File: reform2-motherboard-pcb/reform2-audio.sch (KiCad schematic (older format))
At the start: 32 parts, among them J16 LINE_IN, J21 Conn_01x04, J7 SJ-43516-SMT, U3 WM8960

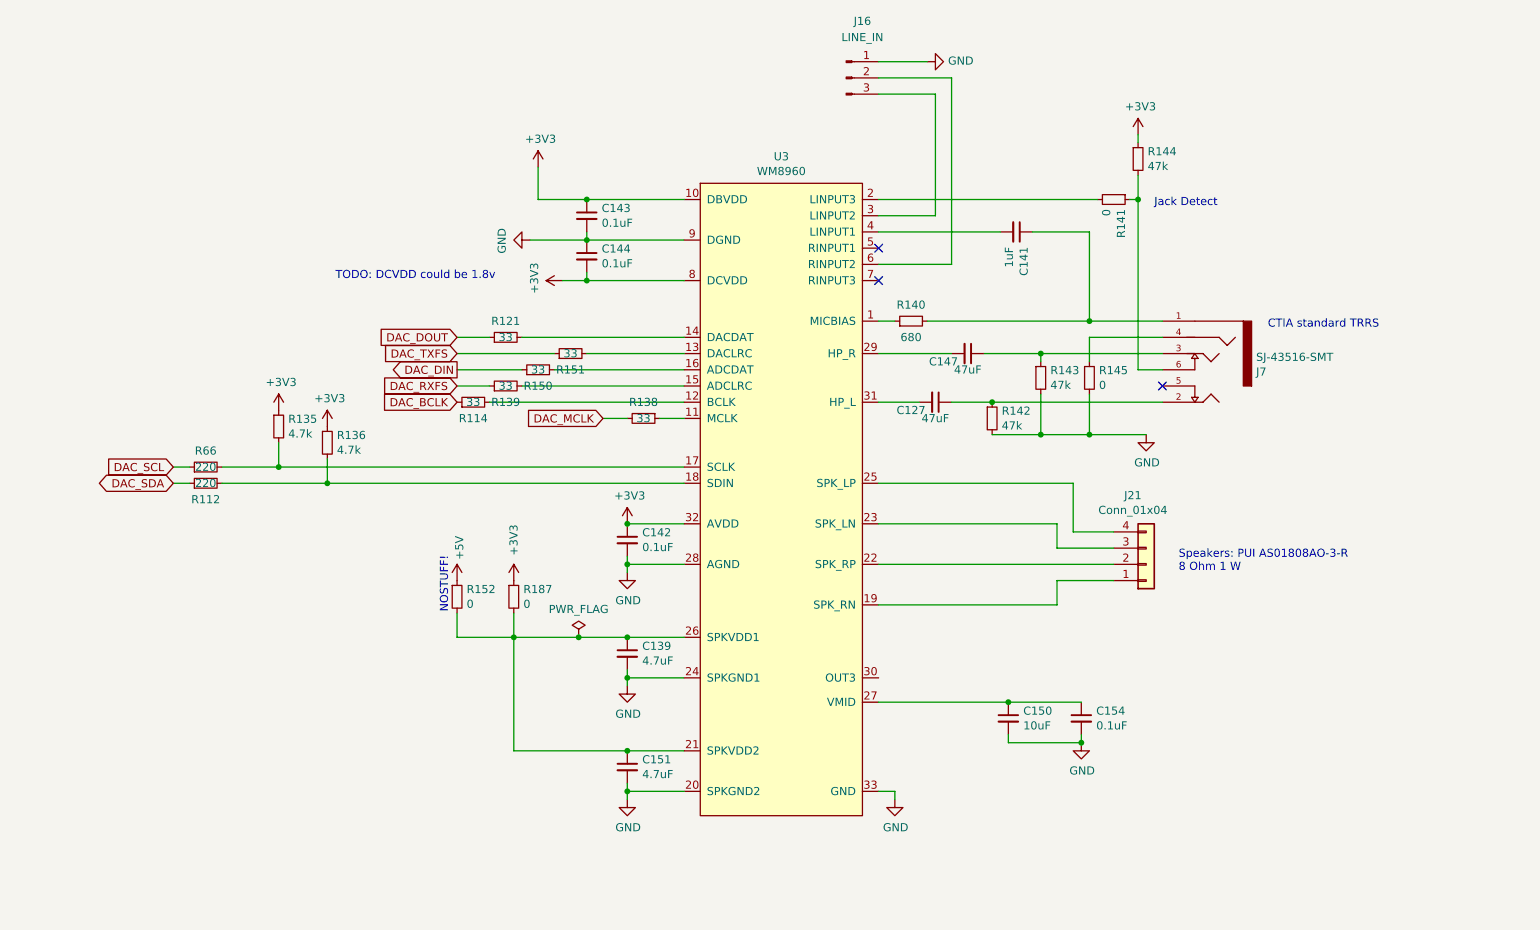
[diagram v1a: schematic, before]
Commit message: reform2-motherboard: version D-4 finished; fixes critical D-3 bugs; adds PCIe refclk termination, speaker output filter stage, pcie0 3v3 load switch, imx reset line to lpc, charge current control line to lpc
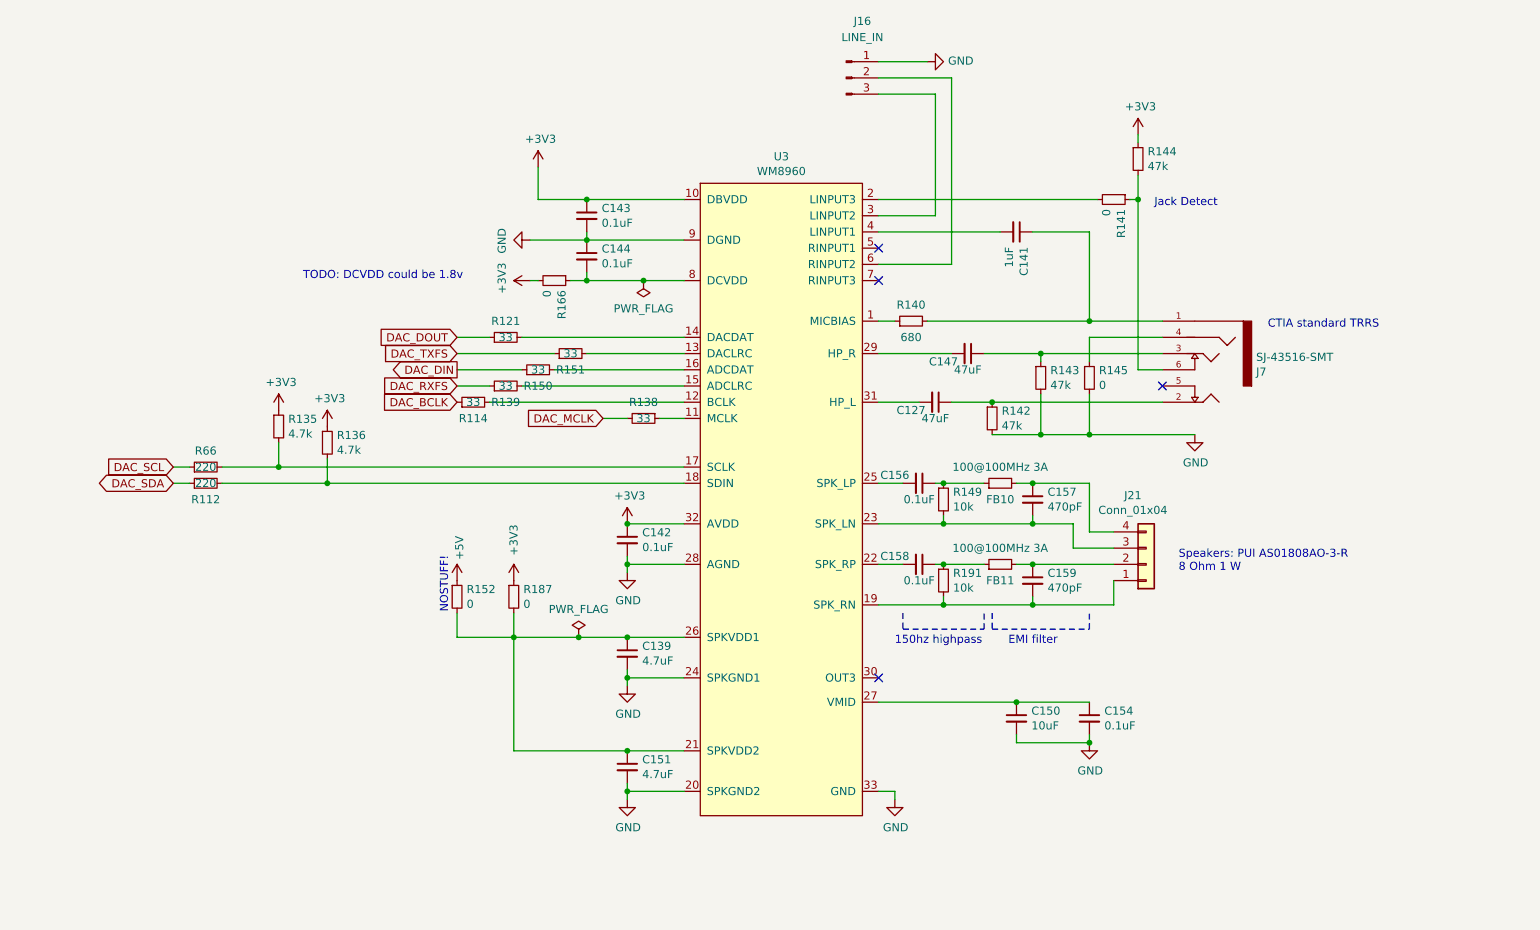
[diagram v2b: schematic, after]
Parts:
- added C156, C158: 0.1uF, Capacitor_SMD:C_0603_1608Metric, symbol Device:C_Small
- added C157, C159: 470pF, Capacitor_SMD:C_0603_1608Metric, symbol Device:C_Small
- added FB10, FB11: 100@100MHz 3A, Inductor_SMD:L_0603_1608Metric, symbol Device:R_Small
- added R149, R191: 10k, Resistor_SMD:R_0603_1608Metric, symbol Device:R_Small
- added R166: 0, Resistor_SMD:R_0603_1608Metric, symbol Device:R_Small
- J16, R152: DNP (none) -> y
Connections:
- net +3V3: now also R166.2; no longer C144.2, U3.8 (DCVDD)
- net at J21.1 (Pin_1), U3.19 (SPK_RN): now also C159.2, R191.2
- net at U3.22 (SPK_RP): now also C158.2; no longer J21.2 (Pin_2)
- net at J21.3 (Pin_3), U3.23 (SPK_LN): now also C157.2, R149.2
- net at U3.25 (SPK_LP): now also C156.2; no longer J21.4 (Pin_4)
- new net: C156.1, FB10.1, R149.1
- new net: C158.1, FB11.1, R191.1
- new net: C144.2, R166.1, U3.8 (DCVDD)
- new net: C157.1, FB10.2, J21.4 (Pin_4)
- new net: C159.1, FB11.2, J21.2 (Pin_2)
- no-connect marks 3 -> 4
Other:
- note added: "150hz highpass"
- note added: "EMI filter"
- moved on the sheet: C150, C154

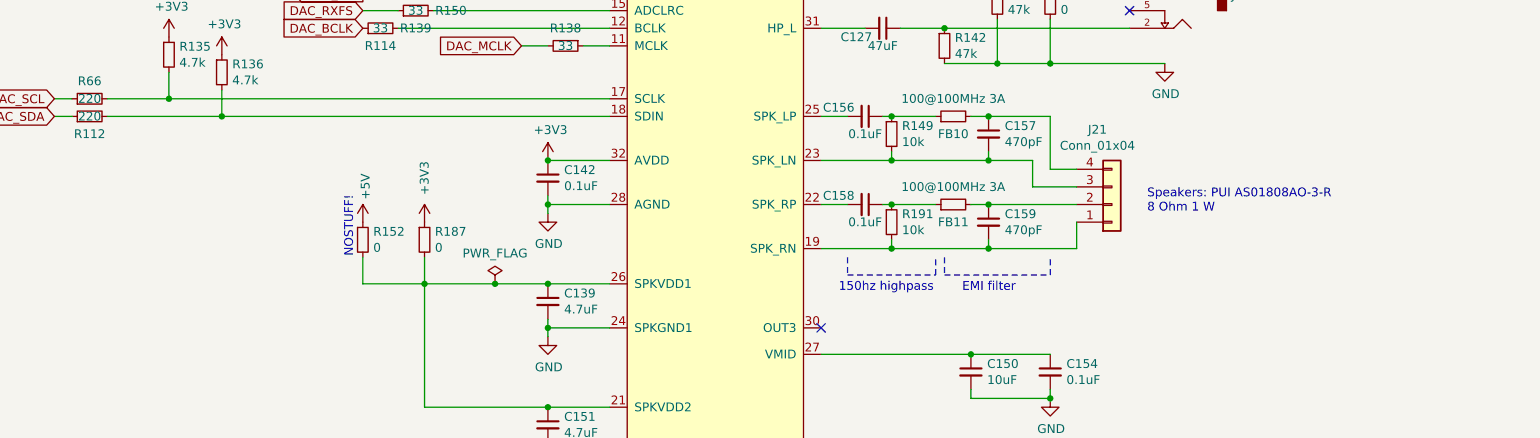
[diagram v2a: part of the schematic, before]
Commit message: WIP: reform2-motherboard: audio output filter work and notes
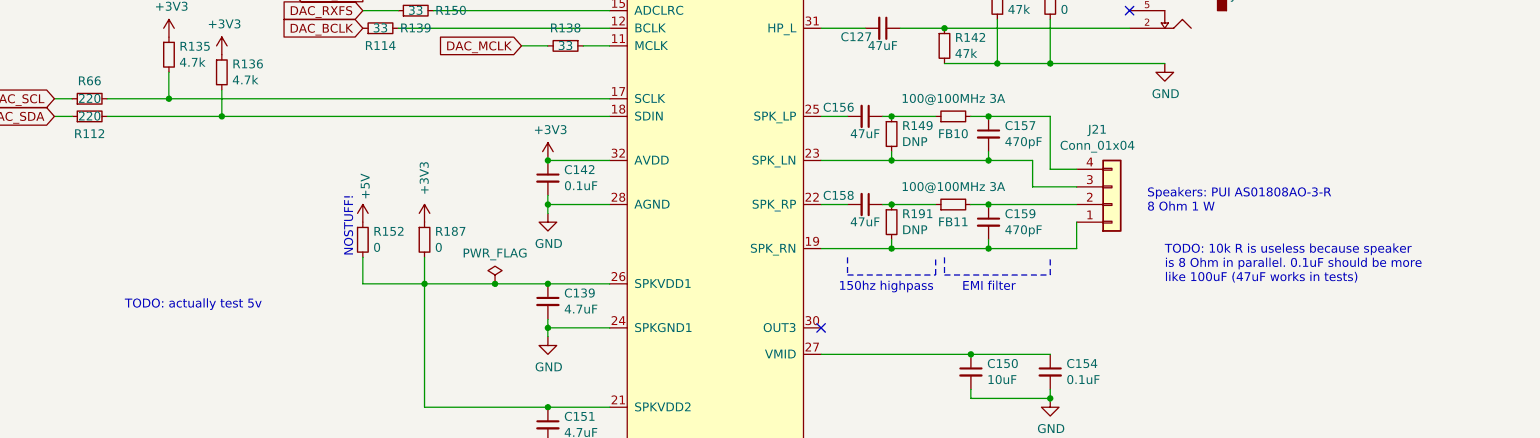
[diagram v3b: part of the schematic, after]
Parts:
- C156, C158: value 0.1uF -> 47uF
- R149, R191: value 10k -> DNP; Checked y -> n; Manufacturer_No RC0603FR-0710KL -> (none)
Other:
- note added: "TODO: 10k R is useless because speaker\nis 8 Ohm in parallel. 0.1uF should be more\nlike 100uF (47uF works in tests)"
- note added: "TODO: actually test 5v"
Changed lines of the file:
@@
 P 6700 3650
 F 0 "C156" V 6650 3500 50  0000 C CNN
-F 1 "0.1uF" V 6800 3650 50  0000 C CNN
+F 1 "47uF" V 6800 3650 50  0000 C CNN
 F 2 "Capacitor_SMD:C_0603_1608Metric" H 6700 3650 50  0001 C CNN
 F 3 "~" H 6700 3650 50  0001 C CNN
@@
 P 6850 3750
 F 0 "R149" H 6909 3796 50  0000 L CNN
-F 1 "10k" H 6909 3705 50  0000 L CNN
+F 1 "DNP" H 6909 3705 50  0000 L CNN
 F 2 "Resistor_SMD:R_0603_1608Metric" H 6850 3750 50  0001 C CNN
 F 3 "~" H 6850 3750 50  0001 C CNN
 F 4 "Yageo" H 6850 3750 50  0001 C CNN "Manufacturer"
-F 5 "RC0603FR-0710KL" H 6850 3750 50  0001 C CNN "Manufacturer_No"
+F 5 "" H 6850 3750 50  0001 C CNN "Manufacturer_No"
 F 6 "Mouser" H 6850 3750 50  0001 C CNN "Distributor"
-F 7 "y" H 6850 3750 50  0001 C CNN "Checked"
+F 7 "n" H 6850 3750 50  0001 C CNN "Checked"
 	1    6850 3750
 	1    0    0    -1
@@
 P 6700 4150
 F 0 "C158" V 6650 4000 50  0000 C CNN
-F 1 "0.1uF" V 6800 4150 50  0000 C CNN
+F 1 "47uF" V 6800 4150 50  0000 C CNN
 F 2 "Capacitor_SMD:C_0603_1608Metric" H 6700 4150 50  0001 C CNN
 F 3 "~" H 6700 4150 50  0001 C CNN
@@
 P 6850 4250
 F 0 "R191" H 6909 4296 50  0000 L CNN
-F 1 "10k" H 6909 4205 50  0000 L CNN
+F 1 "DNP" H 6909 4205 50  0000 L CNN
 F 2 "Resistor_SMD:R_0603_1608Metric" H 6850 4250 50  0001 C CNN
 F 3 "~" H 6850 4250 50  0001 C CNN
 F 4 "Yageo" H 6850 4250 50  0001 C CNN "Manufacturer"
-F 5 "RC0603FR-0710KL" H 6850 4250 50  0001 C CNN "Manufacturer_No"
+F 5 "" H 6850 4250 50  0001 C CNN "Manufacturer_No"
 F 6 "Mouser" H 6850 4250 50  0001 C CNN "Distributor"
-F 7 "y" H 6850 4250 50  0001 C CNN "Checked"
+F 7 "n" H 6850 4250 50  0001 C CNN "Checked"
 	1    6850 4250
 	1    0    0    -1
@@
 Wire Wire Line
 	5000 2400 4650 2400
+Text Notes 8400 4600 0    50   ~ 0
+TODO: 10k R is useless because speaker\nis 8 Ohm in parallel. 0.1uF should be more\nlike 100uF (47uF works in tests)
+Text Notes 2500 4750 0    50   ~ 0
+TODO: actually test 5v
 $EndSCHEMATC

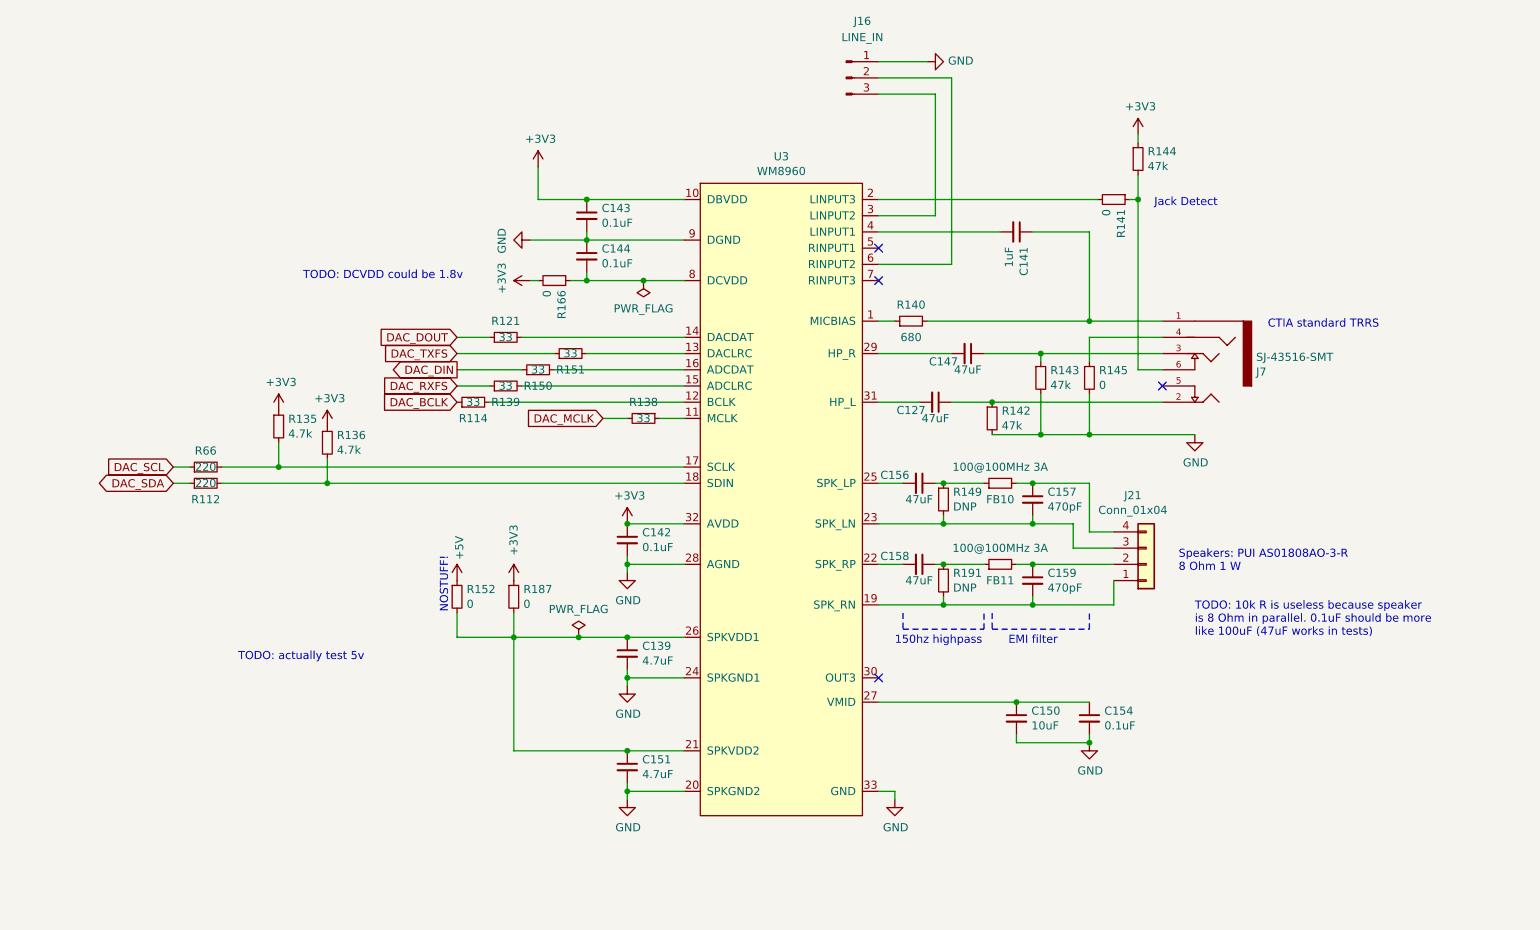
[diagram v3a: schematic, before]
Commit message: reform2-motherboard: first R-1 snapshot. main changes: EMI, ESD, audio filter, enable FETs, SHDN fix, more rail switches
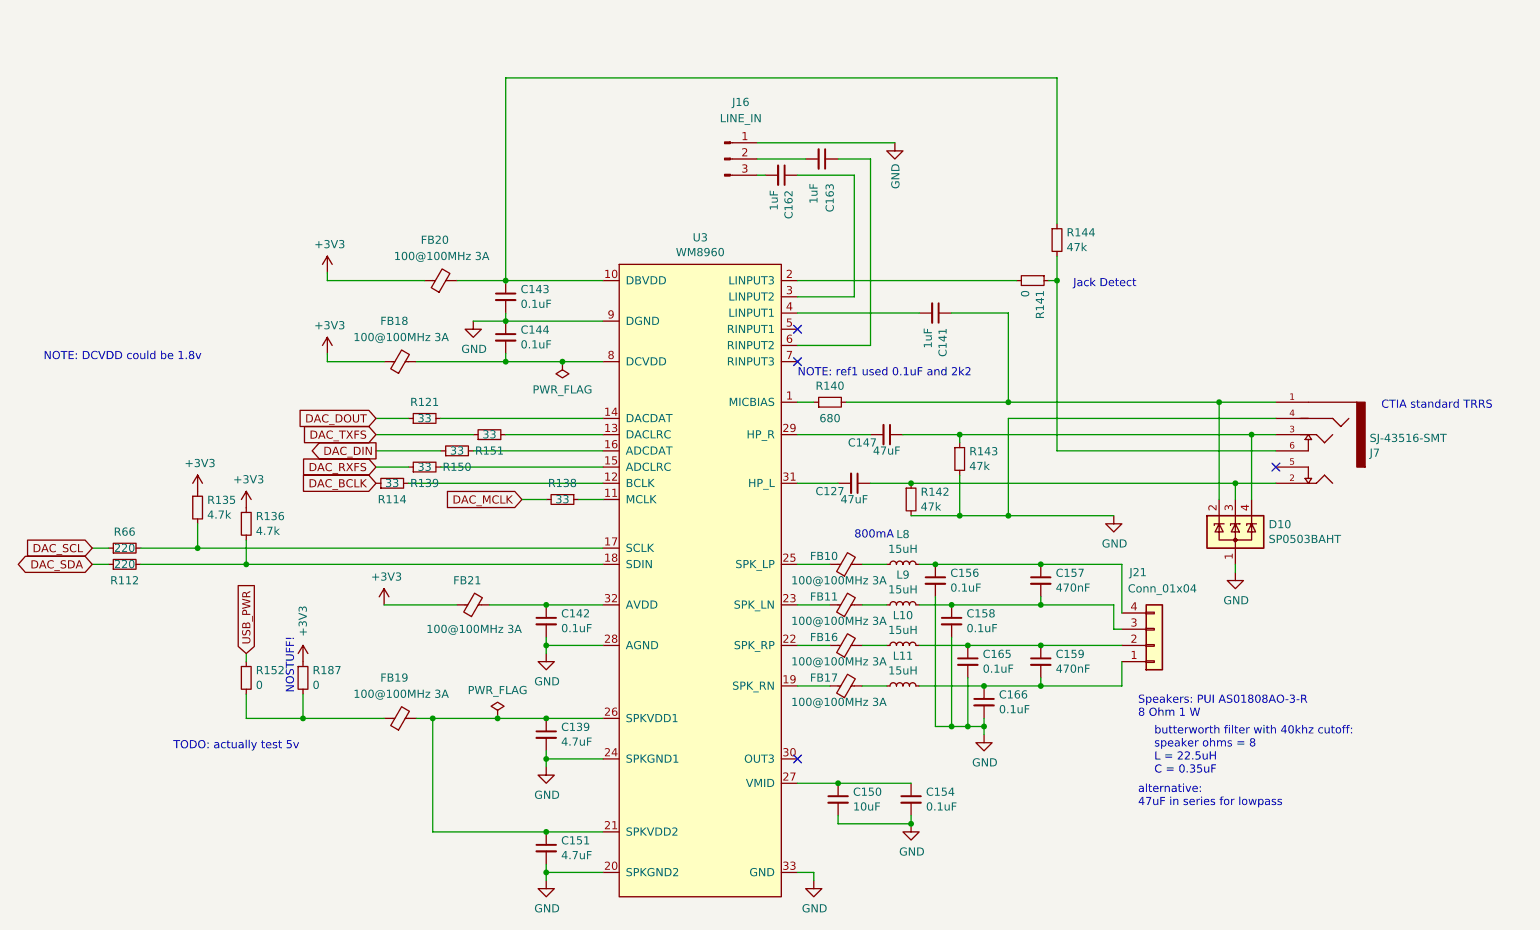
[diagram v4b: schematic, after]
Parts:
- removed FB10, FB11: 100@100MHz 3A, Inductor_SMD:L_0603_1608Metric, symbol Device:R_Small
- removed R145, R166: 0, Resistor_SMD:R_0603_1608Metric, symbol Device:R_Small
- removed R149, R191: DNP, Resistor_SMD:R_0603_1608Metric, symbol Device:R_Small
- added C162, C163: 1uF, Capacitor_SMD:C_0603_1608Metric, symbol Device:C_Small
- added C165, C166: 0.1uF, Capacitor_SMD:C_0603_1608Metric, symbol Device:C_Small
- added D10: SP0503BAHT, Package_TO_SOT_SMD:SOT-143, symbol Power_Protection:SP0503BAHT
- added FB10, FB11, FB16, FB17, FB18, FB19, FB20, FB21: 100@100MHz 3A, Inductor_SMD:L_0603_1608Metric, symbol Device:Ferrite_Bead_Small
- added L10, L11, L8, L9: 15uH, Inductor_SMD:L_1210_3225Metric, symbol Device:L_Small
- C156, C158: value 47uF -> 0.1uF; Checked y -> (none); Manufacturer Yageo -> (none); Manufacturer_No CC0603JPX7R9BB104 -> (none)
- C157, C159: value 470pF -> 470nF; Checked y -> (none); Manufacturer KEMET -> (none); Manufacturer_No C0603C471K8HACAUTO -> (none)
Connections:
- net +3V3: now also FB18.1, FB20.1, FB21.1; no longer C142.1, C143.1, R144.1, U3.10 (DBVDD), U3.32 (AVDD)
- net GND: now also C156.2, C158.2, J7.4 (RING2), C165.2, C166.2, D10.1 (A)
- net at C141.1, J7.1 (SLEEVE), R140.2: now also D10.2 (K)
- net at C127.1, J7.2 (TIP), R142.1: now also D10.3 (K)
- net at C147.1, J7.3 (RING1), R143.1: now also D10.4 (K)
- net at C156.1: now also C157.1, J21.4 (Pin_4), L8.2
- net at U3.25 (SPK_LP): now also FB10.1; no longer C156.2
- net at C157.2, J21.3 (Pin_3): now also C158.1, L9.2; no longer U3.23 (SPK_LN)
- net at U3.22 (SPK_RP): now also FB16.1; no longer C158.2
- net at C159.2, J21.1 (Pin_1): now also C166.1, L11.2; no longer U3.19 (SPK_RN)
- net at C144.2, U3.8 (DCVDD): now also FB18.2
- net at C159.1, J21.2 (Pin_2): now also C165.1, L10.2
- net at C139.1, C151.1, U3.21 (SPKVDD2)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: now also FB19.2; no longer R152.2, R187.2
- net at U3.6 (RINPUT2): now also C163.1; no longer J16.2 (Pin_2)
- net at U3.3 (LINPUT2): now also C162.1; no longer J16.3 (Pin_3)
- net +5V renamed USB_PWR
- new net: C143.1, FB20.2, R144.1, U3.10 (DBVDD)
- new net: C142.1, FB21.2, U3.32 (AVDD)
- new net: C162.2, J16.3 (Pin_3)
- new net: C163.2, J16.2 (Pin_2)
- new net: FB16.2, L10.1
- new net: FB10.2, L8.1
- new net: FB11.2, L9.1
- new net: FB17.2, L11.1
- new net: FB11.1, U3.23 (SPK_LN)
- new net: FB17.1, U3.19 (SPK_RN)
- new net: FB19.1, R152.2, R187.2
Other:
- note added: "800mA"
- note added: "NOTE: DCVDD could be 1.8v"
- note added: "NOTE: ref1 used 0.1uF and 2k2"
- note added: "alternative:\n47uF in series for lowpass"
- note added: "butterworth filter with 40khz cutoff:\nspeaker ohms = 8\nL = 22.5uH\nC = 0.35uF"
- note removed: "150hz highpass"
- note removed: "EMI filter"
- note removed: "TODO: 10k R is useless because speaker\nis 8 Ohm in parallel. 0.1uF should be more\nlike 100uF (47uF works in tests)"
- note removed: "TODO: DCVDD could be 1.8v"
- moved on the sheet: C127, C139, C141, C142, C143, C144, C147, C150, C151, C154, C157, C159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
